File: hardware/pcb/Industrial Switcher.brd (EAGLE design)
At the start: 96.2 x 50 mm, 60 parts, among them IC1 MSP430FR5739, IC2 HY-TFT220, Q1 IRFR5305, Q2 32 kHz, Q3 IRFZ34NS, Q4 IRFZ34NS, Q5 IRFZ34NS, Q6 IRFZ34NS, U1 TDA3664, U2 TPS76933, U3 LT1161CSWPBF

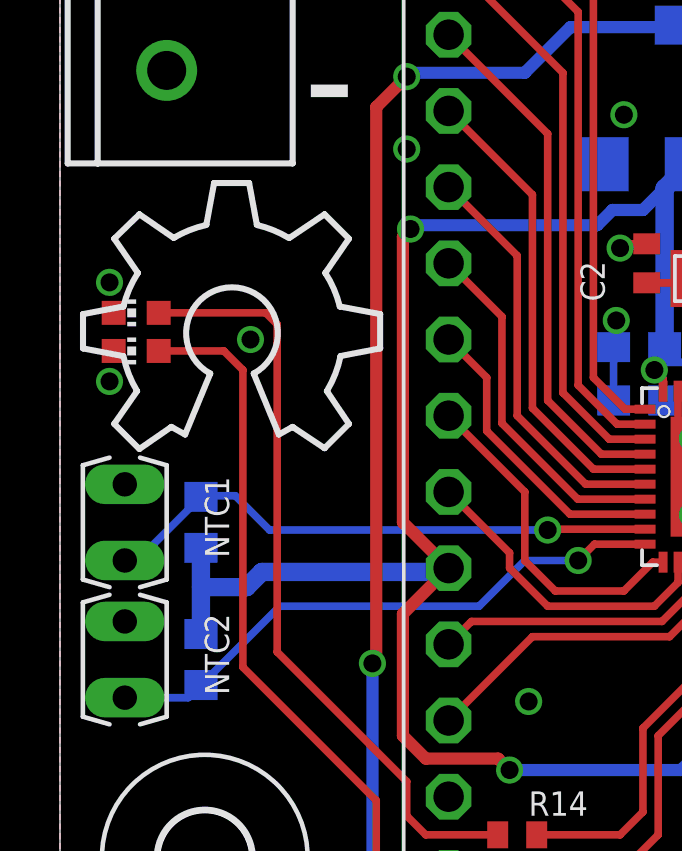
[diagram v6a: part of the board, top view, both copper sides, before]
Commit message: Replaced OSHW logo.
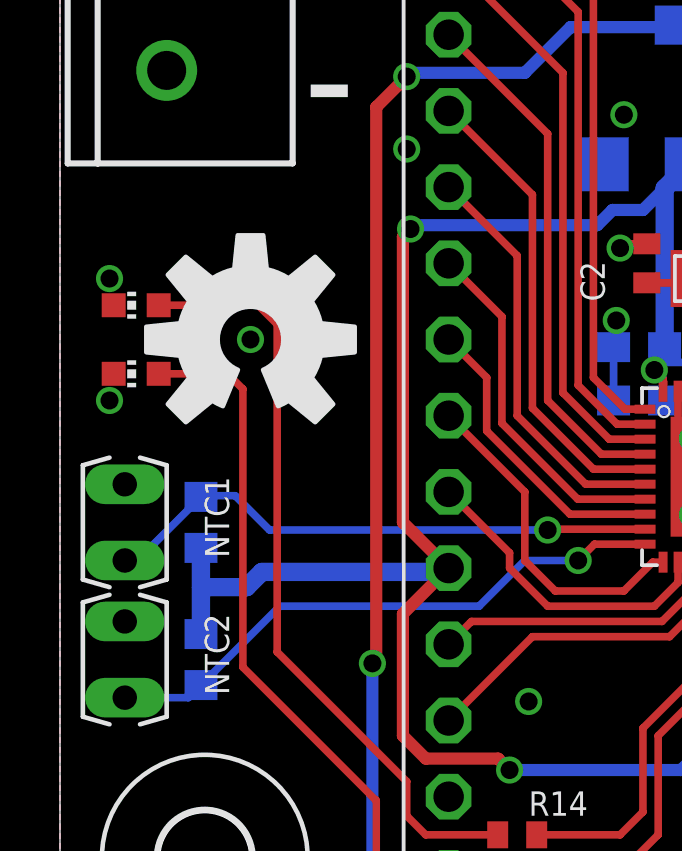
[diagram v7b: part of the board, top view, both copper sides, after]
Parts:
- removed LOGO1: OSHW_LOGO_8MILX0350-NT, OSHW:OSHW_8X350_NOTEXT
- added LOGO2: OSHW-LOGOL, SparkFun-Aesthetics:OSHW-LOGO-L
- moved LED2 0.76 mm to (2.54, 21.0)
- moved LED1 0.25 mm to (2.54, 23.2)
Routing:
- net N$27: track 26.7 -> 26.0 mm
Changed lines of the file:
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@@
 </autorouter>
 <elements>
-<element name="LOGO1" library="OSHW" package="OSHW_8X350_NOTEXT" value="OSHW_LOGO_8MILX0350-NT" x="0.767" y="18.449" smashed="yes"/>
 <element name="NTC2" library="ptc-ntc" package="N640" value="4k7" x="2.159" y="11.43" smashed="yes" rot="R270">
 <attribute name="OC_NEWARK" value="unknown" x="2.159" y="11.43" size="1.778" layer="27" rot="R270" display="off"/>
@@
 <attribute name="VALUE" x="41.059" y="11.204" size="1.016" layer="28" rot="MR90"/>
 </element>
-<element name="LED1" library="led" package="CHIP-LED0603" value="" x="2.54" y="22.987" smashed="yes" rot="R90">
-<attribute name="VALUE" x="3.175" y="24.892" size="1.27" layer="27" rot="R180"/>
-</element>
-<element name="LED2" library="led" package="CHIP-LED0603" value="" x="2.54" y="21.717" smashed="yes" rot="R90">
-<attribute name="VALUE" x="3.175" y="23.622" size="1.27" layer="27" rot="R180"/>
+<element name="LED1" library="led" package="CHIP-LED0603" value="" x="2.54" y="23.241" smashed="yes" rot="R90">
+<attribute name="VALUE" x="3.175" y="25.146" size="1.27" layer="27" rot="R180"/>
+</element>
+<element name="LED2" library="led" package="CHIP-LED0603" value="" x="2.54" y="20.955" smashed="yes" rot="R90">
+<attribute name="VALUE" x="3.175" y="22.86" size="1.27" layer="27" rot="R180"/>
 </element>
 <element name="R14" library="rcl" package="R0402" value="1k" x="15.24" y="5.588" smashed="yes">
@@
 <attribute name="VALUE" x="33.401" y="48.514" size="1.27" layer="28" rot="MR270"/>
 </element>
+<element name="LOGO2" library="SparkFun-Aesthetics" package="OSHW-LOGO-L" value="OSHW-LOGOL" x="6.35" y="22.098"/>
 </elements>
 <signals>
@@
 <wire x1="23.9268" y1="19.1008" x2="23.622" y2="18.796" width="0.254" layer="1"/>
 <via x="6.35" y="22.098" extent="1-16" drill="0.6" shape="octagon"/>
-<via x="1.651" y="20.701" extent="1-16" drill="0.6" shape="octagon"/>
-<via x="1.651" y="24.003" extent="1-16" drill="0.6" shape="octagon"/>
+<via x="1.651" y="20.066" extent="1-16" drill="0.6" shape="octagon"/>
+<via x="1.651" y="24.13" extent="1-16" drill="0.6" shape="octagon"/>
 <contactref element="U$1" pad="3"/>
 <contactref element="U$1" pad="1"/>
@@
 <wire x1="11.557" y1="7.366" x2="7.239" y2="11.684" width="0.254" layer="1"/>
 <wire x1="7.239" y1="11.684" x2="7.239" y2="22.606" width="0.254" layer="1"/>
-<wire x1="7.239" y1="22.606" x2="6.858" y2="22.987" width="0.254" layer="1"/>
-<wire x1="3.29" y1="22.987" x2="6.858" y2="22.987" width="0.254" layer="1"/>
+<wire x1="7.239" y1="22.606" x2="6.604" y2="23.241" width="0.254" layer="1"/>
+<wire x1="3.29" y1="23.241" x2="6.604" y2="23.241" width="0.254" layer="1"/>
 <wire x1="12.192" y1="5.588" x2="14.59" y2="5.588" width="0.254" layer="1"/>
 </signal>
@@
 <wire x1="10.541" y1="3.556" x2="10.541" y2="6.731" width="0.254" layer="1"/>
 <wire x1="10.541" y1="6.731" x2="6.096" y2="11.176" width="0.254" layer="1"/>
-<wire x1="6.096" y1="11.176" x2="6.096" y2="21.082" width="0.254" layer="1"/>
-<wire x1="3.29" y1="21.717" x2="5.461" y2="21.717" width="0.254" layer="1"/>
-<wire x1="5.461" y1="21.717" x2="6.096" y2="21.082" width="0.254" layer="1"/>
+<wire x1="6.096" y1="11.176" x2="6.096" y2="20.447" width="0.254" layer="1"/>
+<wire x1="3.29" y1="20.955" x2="5.588" y2="20.955" width="0.254" layer="1"/>
+<wire x1="5.588" y1="20.955" x2="6.096" y2="20.447" width="0.254" layer="1"/>
 <wire x1="11.049" y1="3.048" x2="14.59" y2="3.048" width="0.254" layer="1"/>
 </signal>
